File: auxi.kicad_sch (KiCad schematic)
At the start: 45 parts

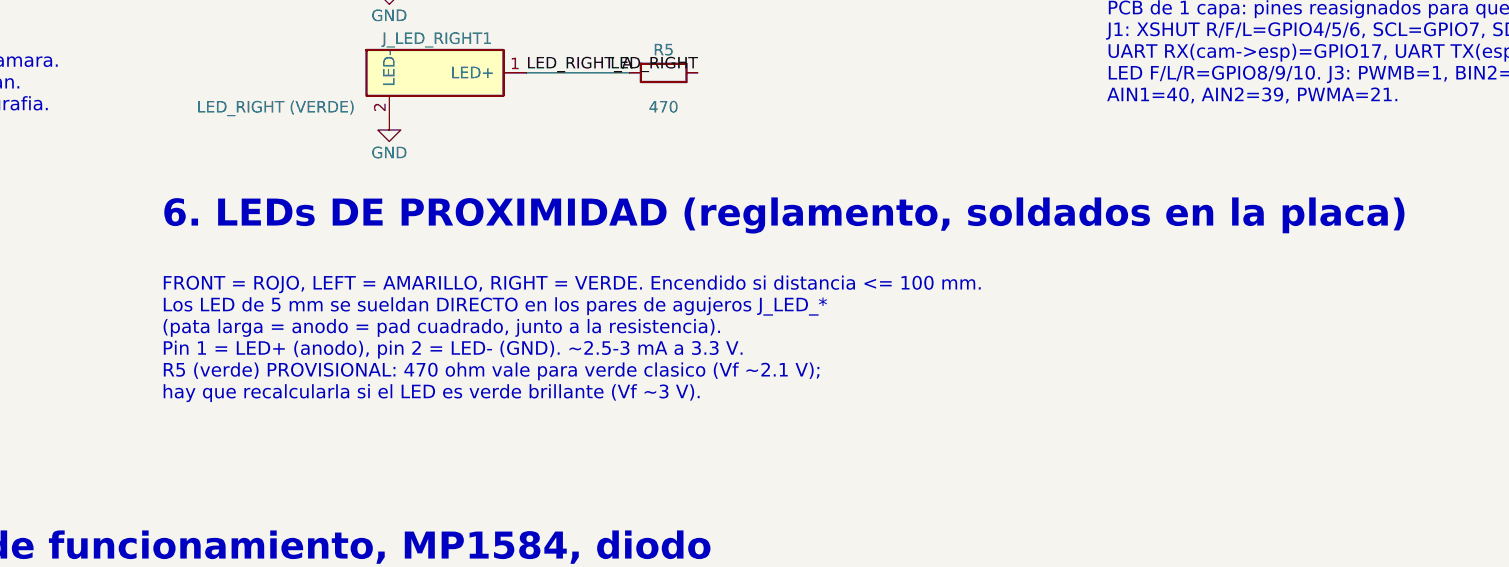
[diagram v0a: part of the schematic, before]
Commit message: Docs: proximity sensors are configured to turn on their LEDs at 15 cm
Co-Authored-By: Claude Sonnet 5.5 <noreply@anthropic.com>
Claude-Session: https://claude.ai/code/session_01HrZukSfyeMd8Be9PGS4Uge
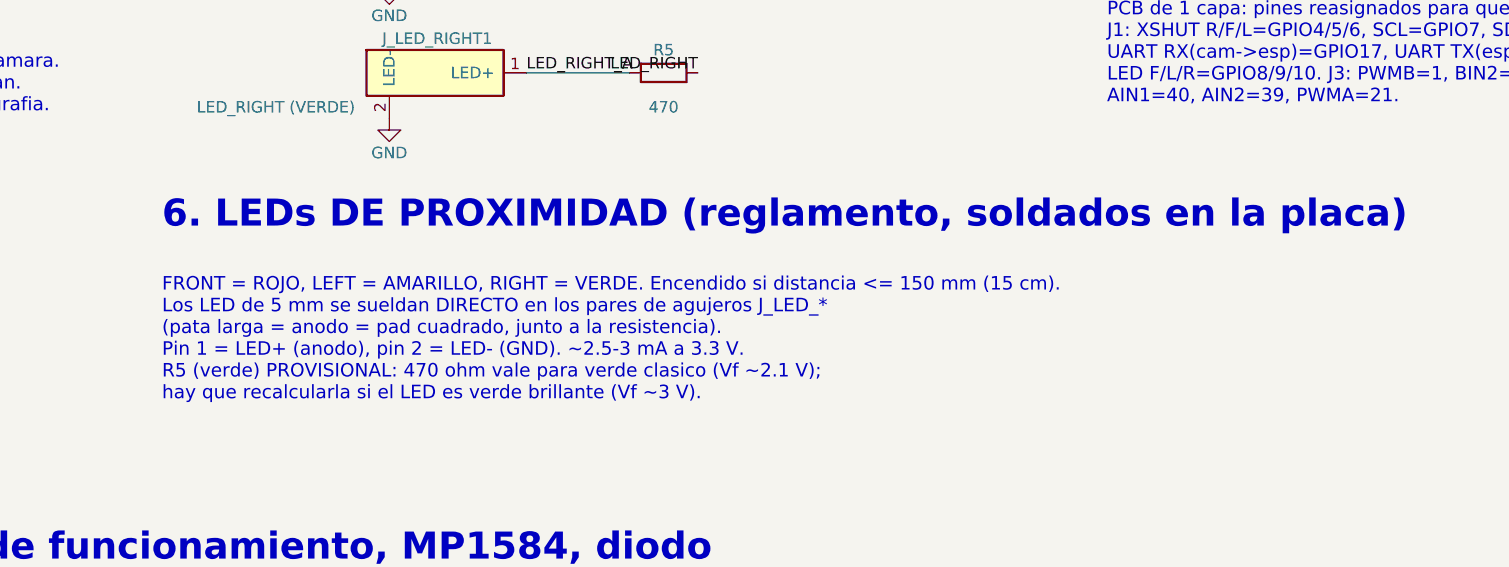
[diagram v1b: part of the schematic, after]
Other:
- note added: "FRONT = ROJO, LEFT = AMARILLO, RIGHT = VERDE. Encendido si distancia <= 150 mm (15 cm). Los LED de 5 mm se sueldan DIRECTO en los pares de agujeros J_LED_* (pata larga = anodo = pad cuadrado, junto a la resistencia). Pin 1 = LED+ (anodo), pin 2 = LED- (GND). ~2.5-3 mA a 3.3 V. R5 (verde) PROVISIONAL: 470 ohm vale para verde clasico (Vf ~2.1 V); hay que recalcularla si el LED es verde brillante (V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"
- note removed: "FRONT = ROJO, LEFT = AMARILLO, RIGHT = VERDE. Encendido si distancia <= 100 mm. Los LED de 5 mm se sueldan DIRECTO en los pares de agujeros J_LED_* (pata larga = anodo = pad cuadrado, junto a la resistencia). Pin 1 = LED+ (anodo), pin 2 = LED- (GND). ~2.5-3 mA a 3.3 V. R5 (verde) PROVISIONAL: 470 ohm vale para verde clasico (Vf ~2.1 V); hay que recalcularla si el LED es verde brillante (Vf ~3 V)."
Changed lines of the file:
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@@
 		)
 	)
-	(text "FRONT = ROJO, LEFT = AMARILLO, RIGHT = VERDE. Encendido si distancia <= 100 mm.\nLos LED de 5 mm se sueldan DIRECTO en los pares de agujeros J_LED_*\n(pata larga = anodo = pad cuadrado, junto a la resistencia).\nPin 1 = LED+ (anodo), pin 2 = LED- (GND). ~2.5-3 mA a 3.3 V.\nR5 (verde) PROVISIONAL: 470 ohm vale para verde clasico (Vf ~2.1 V);\nhay que recalcularla si el LED es verde brillante (Vf ~3 V)."
+	(text "FRONT = ROJO, LEFT = AMARILLO, RIGHT = VERDE. Encendido si distancia <= 150 mm (15 cm).\nLos LED de 5 mm se sueldan DIRECTO en los pares de agujeros J_LED_*\n(pata larga = anodo = pad cuadrado, junto a la resistencia).\nPin 1 = LED+ (anodo), pin 2 = LED- (GND). ~2.5-3 mA a 3.3 V.\nR5 (verde) PROVISIONAL: 470 ohm vale para verde clasico (Vf ~2.1 V);\nhay que recalcularla si el LED es verde brillante (Vf ~3 V)."
 		(exclude_from_sim no)
 		(at 150 222 0)

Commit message: KiCad: SDA=GPIO7 y SCL=GPIO15 segun el firmware
Se renombran las redes SDA/SCL sin mover pistas. En los conectores de
sensor el orden pasa a 3=SCL, 4=SDA.

Co-Authored-By: Claude Sonnet 5.5 <noreply@anthropic.com>
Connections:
- net SCL: now also J_SENSOR_FRONT1.3 (SCL), J_SENSOR_LEFT1.3 (SCL), J_SENSOR_RIGHT1.3 (SCL), U_ESP_J1.8 (GPIO15); no longer J_SENSOR_FRONT1.4 (SCL), J_SENSOR_LEFT1.4 (SCL), J_SENSOR_RIGHT1.4 (SCL), U_ESP_J1.7 (GPIO7)
- net SDA: now also J_SENSOR_FRONT1.4 (SDA), J_SENSOR_LEFT1.4 (SDA), J_SENSOR_RIGHT1.4 (SDA), U_ESP_J1.7 (GPIO7); no longer J_SENSOR_FRONT1.3 (SDA), J_SENSOR_LEFT1.3 (SDA), J_SENSOR_RIGHT1.3 (SDA), U_ESP_J1.8 (GPIO15)
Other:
- note added: "Orden en los 3 conectores: 1 3V3, 2 GND, 3 SCL, 4 SDA, 5 XSHUT. I2C compartido a 100 kHz, cables de 25 cm o menos. Pull-ups I2C: los GY-530 ya los incluyen. Sin pull-ups extra en la placa. Firmware: todos los XSHUT en bajo, activar uno a uno y asignar 0x30, 0x31, 0x32."
- note added: "Pinout oficial Espressif v1.1 - VERIFICAR contra el clon comprado. No usar: GPIO0/3/45/46 (arranque), 19/20 (USB), 43/44 (consola), 35/36/37 (PSRAM octal), 38/48 (LED RGB), 47. Bluetooth: solo BLE (control Xbox por BLE). PCB de 1 capa: pines reasignados para que las pistas no se crucen. J1: XSHUT R/F/L=GPIO4/5/6, SDA=GPIO7, SCL=GPIO15, UART RX(cam->esp)=GPIO17, UART TX(esp->cam)=GPIO18, LED F/L/R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"
- note removed: "Orden en los 3 conectores: 1 3V3, 2 GND, 3 SDA, 4 SCL, 5 XSHUT. I2C compartido a 100 kHz, cables de 25 cm o menos. Pull-ups I2C: los GY-530 ya los incluyen. Sin pull-ups extra en la placa. Firmware: todos los XSHUT en bajo, activar uno a uno y asignar 0x30, 0x31, 0x32."
- note removed: "Pinout oficial Espressif v1.1 - VERIFICAR contra el clon comprado. No usar: GPIO0/3/45/46 (arranque), 19/20 (USB), 43/44 (consola), 35/36/37 (PSRAM octal), 38/48 (LED RGB), 47. Bluetooth: solo BLE (control Xbox por BLE). PCB de 1 capa: pines reasignados para que las pistas no se crucen. J1: XSHUT R/F/L=GPIO4/5/6, SCL=GPIO7, SDA=GPIO15, UART RX(cam->esp)=GPIO17, UART TX(esp->cam)=GPIO18, LED F/L/R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"
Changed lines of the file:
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@@
+		)
+	)
+	(label "SDA"
+		(at 251.46 115.57 180)
+		(effects
+			(font
+				(size 1.27 1.27)
+			)
+			(justify right bottom)
 		)
 	)
 	(label "SCL"
-		(at 251.46 115.57 180)
-		(effects
-			(font
-				(size 1.27 1.27)
-			)
-			(justify right bottom)
-		)
-	)
-	(label "SDA"
 		(at 251.46 118.11 180)
 		(effects
@@
 		)
 	)
+	(label "SCL"
+		(at 165.1 43.18 0)
+		(effects
+			(font
+				(size 1.27 1.27)
+			)
+			(justify left bottom)
+		)
+	)
+	(label "SCL"
+		(at 165.1 68.58 0)
+		(effects
+			(font
+				(size 1.27 1.27)
+			)
+			(justify left bottom)
+		)
+	)
+	(label "SCL"
+		(at 165.1 93.98 0)
+		(effects
+			(font
+				(size 1.27 1.27)
+			)
+			(justify left bottom)
+		)
+	)
 	(label "SDA"
-		(at 165.1 43.18 0)
+		(at 165.1 45.72 0)
 		(effects
 			(font
@@
 	)
 	(label "SDA"
-		(at 165.1 68.58 0)
+		(at 165.1 71.12 0)
 		(effects
 			(font
@@
 	)
 	(label "SDA"
-		(at 165.1 93.98 0)
-		(effects
-			(font
-				(size 1.27 1.27)
-			)
-			(justify left bottom)
-		)
-	)
-	(label "SCL"
-		(at 165.1 45.72 0)
-		(effects
-			(font
-				(size 1.27 1.27)
-			)
-			(justify left bottom)
-		)
-	)
-	(label "SCL"
-		(at 165.1 71.12 0)
-		(effects
-			(font
-				(size 1.27 1.27)
-			)
-			(justify left bottom)
-		)
-	)
-	(label "SCL"
 		(at 165.1 96.52 0)
 		(effects
@@
 		)
 	)
-	(text "Pinout oficial Espressif v1.1 - VERIFICAR contra el clon comprado.\nNo usar: GPIO0/3/45/46 (arranque), 19/20 (USB), 43/44 (consola),\n35/36/37 (PSRAM octal), 38/48 (LED RGB), 47.\nBluetooth: solo BLE (control Xbox por BLE).\nPCB de 1 capa: pines reasignados para que las pistas no se crucen.\nJ1: XSHUT R/F/L=GPIO4/5/6, SCL=GPIO7, SDA=GPIO15,\nUART RX(cam->esp)=GPIO17, UART TX(esp->cam)=GPIO18,\nLED F/L/R=GPIO8/9/10. J3: PWMB=1, BIN2=2, BIN1=42, STBY=41,\nAIN1=40, AIN2=39, PWMA=21."
+	(text "Pinout oficial Espressif v1.1 - VERIFICAR contra el clon comprado.\nNo usar: GPIO0/3/45/46 (arranque), 19/20 (USB), 43/44 (consola),\n35/36/37 (PSRAM octal), 38/48 (LED RGB), 47.\nBluetooth: solo BLE (control Xbox por BLE).\nPCB de 1 capa: pines reasignados para que las pistas no se crucen.\nJ1: XSHUT R/F/L=GPIO4/5/6, SDA=GPIO7, SCL=GPIO15,\nUART RX(cam->esp)=GPIO17, UART TX(esp->cam)=GPIO18,\nLED F/L/R=GPIO8/9/10. J3: PWMB=1, BIN2=2, BIN1=42, STBY=41,\nAIN1=40, AIN2=39, PWMA=21."
 		(exclude_from_sim no)
 		(at 255 189.00 0)
@@
 		)
 	)
-	(text "Orden en los 3 conectores:\n1 3V3, 2 GND, 3 SDA, 4 SCL, 5 XSHUT.\nI2C compartido a 100 kHz,\ncables de 25 cm o menos.\nPull-ups I2C: los GY-530 ya los\nincluyen. Sin pull-ups extra en la placa.\nFirmware: todos los XSHUT en bajo,\nactivar uno a uno y asignar\n0x30, 0x31, 0x32."
+	(text "Orden en los 3 conectores:\n1 3V3, 2 GND, 3 SCL, 4 SDA, 5 XSHUT.\nI2C compartido a 100 kHz,\ncables de 25 cm o menos.\nPull-ups I2C: los GY-530 ya los\nincluyen. Sin pull-ups extra en la placa.\nFirmware: todos los XSHUT en bajo,\nactivar uno a uno y asignar\n0x30, 0x31, 0x32."
 		(exclude_from_sim no)
 		(at 30 70 0)
@@
 			)
 		)
-		(property "Description" "Conector JST-XH 5P para modulo VL53L0X (GY-530). Pines: 1 3V3, 2 GND, 3 SDA, 4 SCL, 5 XSHUT."
+		(property "Description" "Conector JST-XH 5P para modulo VL53L0X (GY-530). Pines: 1 3V3, 2 GND, 3 SCL, 4 SDA, 5 XSHUT."
 			(at 144.78 45.72 0)
 			(hide yes)
@@
 			)
 		)
-		(property "Description" "Conector JST-XH 5P para modulo VL53L0X (GY-530). Pines: 1 3V3, 2 GND, 3 SDA, 4 SCL, 5 XSHUT."
+		(property "Description" "Conector JST-XH 5P para modulo VL53L0X (GY-530). Pines: 1 3V3, 2 GND, 3 SCL, 4 SDA, 5 XSHUT."
 			(at 144.78 71.12 0)
 			(hide yes)
@@
 			)
 		)
-		(property "Description" "Conector JST-XH 5P para modulo VL53L0X (GY-530). Pines: 1 3V3, 2 GND, 3 SDA, 4 SCL, 5 XSHUT."
+		(property "Description" "Conector JST-XH 5P para modulo VL53L0X (GY-530). Pines: 1 3V3, 2 GND, 3 SCL, 4 SDA, 5 XSHUT."
 			(at 144.78 96.52 0)
 			(hide yes)
